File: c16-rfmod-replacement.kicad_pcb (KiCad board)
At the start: 2 copper layers, 46.6 x 38.6 mm, 21 parts, among them J1 Conn_01x04_Pin, J2 Conn_01x04_Pin, J3 Mini-DIN-4, U1 THS7314, U2 LD1117S33TR_SOT223

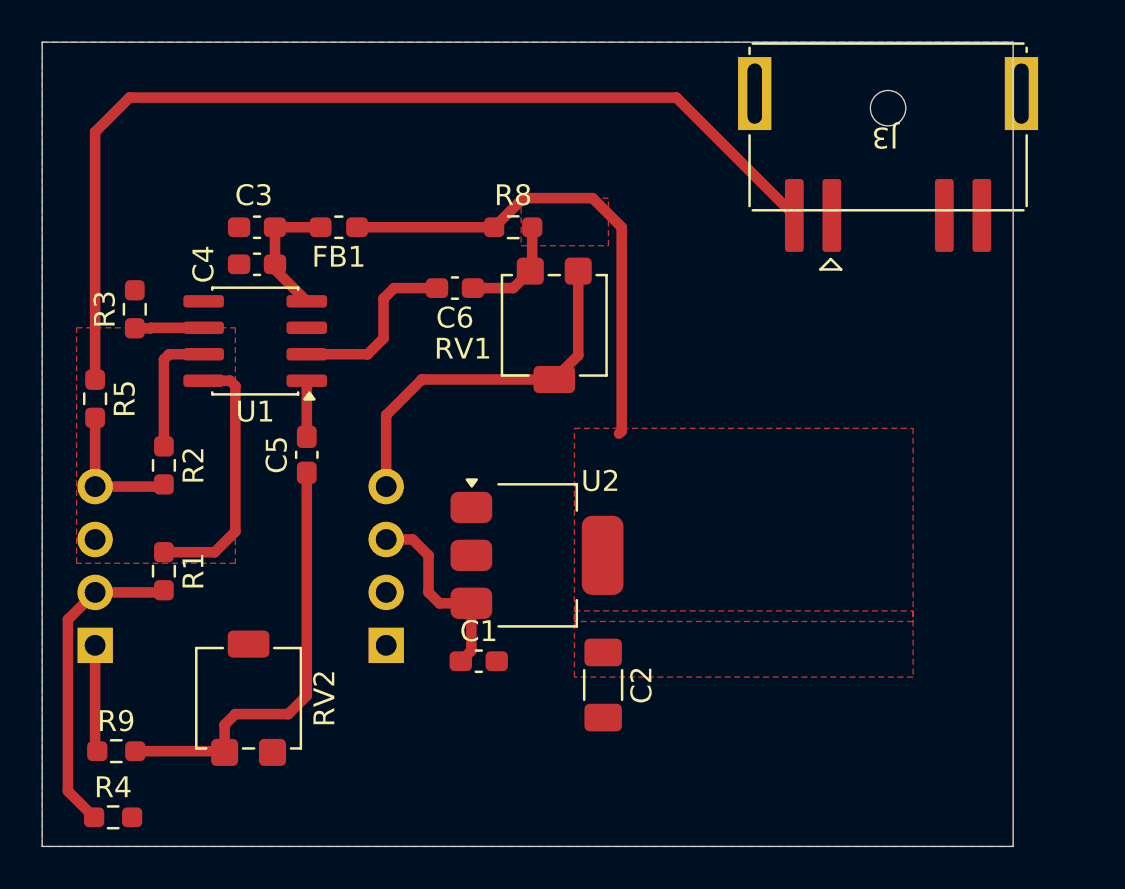
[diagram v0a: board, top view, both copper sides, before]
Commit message: C16 RF modulator replacement Rev. B
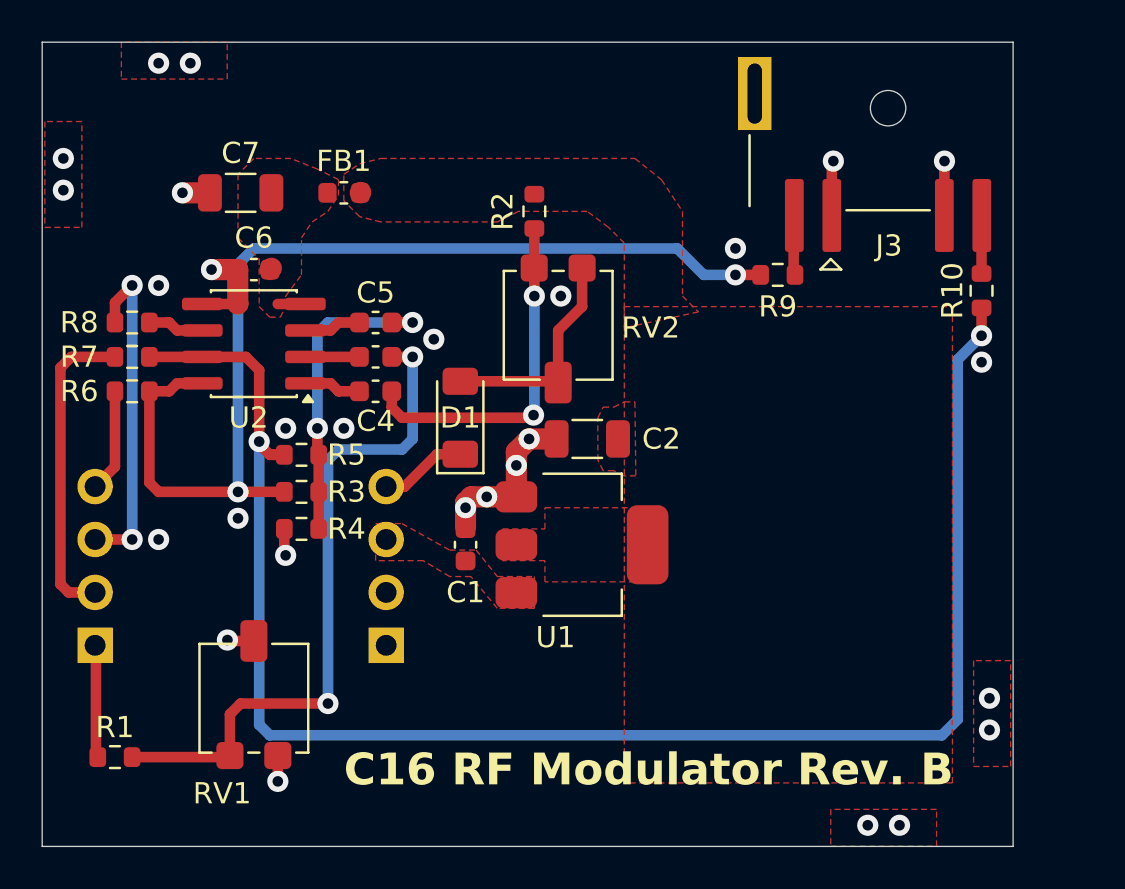
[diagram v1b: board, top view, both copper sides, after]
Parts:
- added C5: 100n, Capacitor_SMD:C_0603_1608Metric, F.Cu at (143.0, 101.9)
- added D1: 1N4148WT, Diode_SMD:D_MiniMELF, F.Cu at (147.1, 106.4)
- added R10: 75R, Resistor_SMD:R_0603_1608Metric, F.Cu at (172.1, 100.3)
- added R8: 75R, Resistor_SMD:R_0603_1608Metric, F.Cu at (131.3, 101.9)
- added R9: 75R, Resistor_SMD:R_0603_1608Metric, F.Cu at (162.3, 99.6)
- C1: footprint Capacitor_SMD:C_0603_1608Metric_Pad1.08x0.95mm_HandSolder -> Capacitor_SMD:C_0603_1608Metric
- C2: footprint Capacitor_SMD:C_1206_3216Metric_Pad1.33x1.80mm_HandSolder -> Capacitor_SMD:C_1206_3216Metric
- C3: renamed from C5; footprint Capacitor_SMD:C_0603_1608Metric_Pad1.08x0.95mm_HandSolder -> Capacitor_SMD:C_0603_1608Metric
- C4: renamed from C6; footprint Capacitor_SMD:C_0603_1608Metric_Pad1.08x0.95mm_HandSolder -> Capacitor_SMD:C_0603_1608Metric
- C6: renamed from C3; footprint Capacitor_SMD:C_0603_1608Metric_Pad1.08x0.95mm_HandSolder -> Capacitor_SMD:C_0603_1608Metric
- C7: renamed from C4; value 1u -> 47u; footprint Capacitor_SMD:C_0603_1608Metric_Pad1.08x0.95mm_HandSolder -> Capacitor_SMD:C_1206_3216Metric
- FB1: value FerriteBead_Small -> ~; footprint Inductor_SMD:L_0603_1608Metric_Pad1.05x0.95mm_HandSolder -> Inductor_SMD:L_0603_1608Metric
- J1, J2: value Conn_01x04_Pin -> C16_RFCon
- J3: value Mini-DIN-4 -> S-Video Out
- R1: renamed from R9; footprint Resistor_SMD:R_0603_1608Metric_Pad0.98x0.95mm_HandSolder -> Resistor_SMD:R_0603_1608Metric
- R2: renamed from R8; value 1k -> 220; footprint Resistor_SMD:R_0603_1608Metric_Pad0.98x0.95mm_HandSolder -> Resistor_SMD:R_0603_1608Metric
- R3: value 150R -> tbd; footprint Resistor_SMD:R_0603_1608Metric_Pad0.98x0.95mm_HandSolder -> Resistor_SMD:R_0603_1608Metric
- R4, R5: value 0 -> tbd; footprint Resistor_SMD:R_0603_1608Metric_Pad0.98x0.95mm_HandSolder -> Resistor_SMD:R_0603_1608Metric
- R6: renamed from R1; footprint Resistor_SMD:R_0603_1608Metric_Pad0.98x0.95mm_HandSolder -> Resistor_SMD:R_0603_1608Metric
- R7: renamed from R2; footprint Resistor_SMD:R_0603_1608Metric_Pad0.98x0.95mm_HandSolder -> Resistor_SMD:R_0603_1608Metric
- RV1: renamed from RV2; footprint Potentiometer_SMD:Potentiometer_Bourns_3214G_Horizontal -> Potentiometer_SMD:Potentiometer_Vishay_TS53YL_Vertical
- RV2: renamed from RV1; value 500 -> 1k; footprint Potentiometer_SMD:Potentiometer_Bourns_3214G_Horizontal -> Potentiometer_SMD:Potentiometer_Vishay_TS53YL_Vertical
- U1: renamed from U2; value LD1117S33TR_SOT223 -> LD1117S33TR
- moved R4 16.5 mm to (139.4, 111.8)
- moved R3 11.9 mm to (139.4, 110.0), turned to 180 degrees
- moved C2 11.8 mm to (153.2, 107.4), turned to 180 degrees
- moved R5 10.3 mm to (139.4, 108.2), turned to 180 degrees
- moved R6 8.77 mm to (131.3, 105.2), turned to 180 degrees
- moved C4 6.25 mm to (143.0, 105.2)
- moved C3 5.74 mm to (143.0, 103.5), turned to 180 degrees
- moved C1 5.62 mm to (147.3, 112.5), turned to 90 degrees
- moved R7 5.43 mm to (131.3, 103.5), turned to 180 degrees
- moved C7 3.52 mm to (136.5, 95.6)
- moved U1 2.22 mm to (152.9, 112.5)
- moved C6 2.04 mm to (137.2, 99.3)
- moved FB1 1.67 mm to (141.5, 95.6)
- moved R2 1.27 mm to (150.6, 96.5), turned to -90 degrees
- moved R1 0.29 mm to (130.5, 122.7)
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- renumbered U1 to U2
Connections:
- net /Chroma_IN renamed /Chroma_C16
- net Net-(C5-Pad1) renamed /Chroma_VD
- net Net-(C6-Pad1) renamed /Luma_VDOUT
- net Net-(U1-V_{S+}) renamed +3.3V_filt
- C3 pad 2: Net-(U1-CH1_IN) -> /Chroma_InTHS
- C4 pad 2: Net-(U1-CH2_IN) -> /Luma_InTHS
- J1 pad 2: /Audio_IN -> unconnected-(J1-Pin_2-Pad2)
- J1 pad 4: /Luma_IN -> /Luma_C16
- J2 pad 2: /Chroma_OUT -> Chroma_Out
- J2 pad 3: /Comp_OUT -> Comp_Out
- J2 pad 4: /Luma_Out -> Luma_Out
- J3 pad 3: Net-(J3-Pad3) -> /Luma_OutSVideo
- J3 pad 4: Net-(J3-Pad4) -> /Chroma_OutSVideo
- R3 pad 1: Net-(U1-CH3_OUT) -> /Comp_FB
- R3 pad 2: GND -> /Luma_OutTHS
- R4 pad 1: /Chroma_OUT -> GND
- R4 pad 2: Net-(J3-Pad4) -> /Comp_FB
- R5 pad 1: Net-(J3-Pad3) -> /Comp_FB
- R5 pad 2: /Luma_Out -> /Chroma_OutTHS
- R6 pad 1: Net-(U1-CH1_OUT) -> /Luma_OutTHS
- R6 pad 2: /Chroma_OUT -> Luma_Out
- R7 pad 1: Net-(U1-CH2_OUT) -> /Chroma_OutTHS
- R7 pad 2: /Luma_Out -> Chroma_Out
- RV2 pad 2: /Luma_IN -> /Luma_VDIN
- RV2 pad 3: /Luma_IN -> /Luma_VDIN
- U2 pad 1: Net-(U1-CH1_IN) -> /Luma_InTHS
- U2 pad 2: Net-(U1-CH2_IN) -> /Chroma_InTHS
- U2 pad 3: GND -> /Comp_InTHS
- U2 pad 6: Net-(U1-CH3_OUT) -> /Comp_OutTHS
- U2 pad 7: Net-(U1-CH2_OUT) -> /Chroma_OutTHS
- U2 pad 8: Net-(U1-CH1_OUT) -> /Luma_OutTHS
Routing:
- net /Chroma_OutTHS: track 0.00 -> 78.9 mm, vias 0 -> 2
- net /Luma_OutTHS: track 0.00 -> 50.6 mm, vias 0 -> 2
- net Net-(J3-Pad3): track 48.5 -> 0.00 mm
- net +3.3V: track 23.8 -> 0.03 mm
- net GND: track 0.00 -> 23.0 mm, vias 0 -> 28
- net /Luma_IN: track 17.9 -> 0.00 mm
- net Comp_Out: track 0.00 -> 16.1 mm, vias 0 -> 2
- net /Comp_FB: track 0.00 -> 15.2 mm, vias 0 -> 2
- net /Chroma_OUT: track 15.2 -> 0.00 mm
- net Chroma_Out: track 0.00 -> 15.0 mm
- net Net-(U1-CH1_OUT): track 12.5 -> 0.00 mm
- net /Chroma_VD: track 20.9 -> 32.6 mm, vias 0 -> 2
- net /Luma_VDOUT: track 5.23 -> 17.0 mm, vias 0 -> 2
- net /Luma_VDIN: track 0.00 -> 10.7 mm
- net +5V: track 9.41 -> 0.00 mm
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- added copper zone on F.Cu, net +3.3V_filt
- added copper zone on F.Cu, net +5V
- added copper zone on In1.Cu, net GND
- added copper zone on In2.Cu, net GND
- removed copper zone on F.Cu, net (none)
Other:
- copper layers 2 -> 4
- board text added: "C16 RF Modulator Rev. B"

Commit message: Rev. C - Dual Output Amplifier
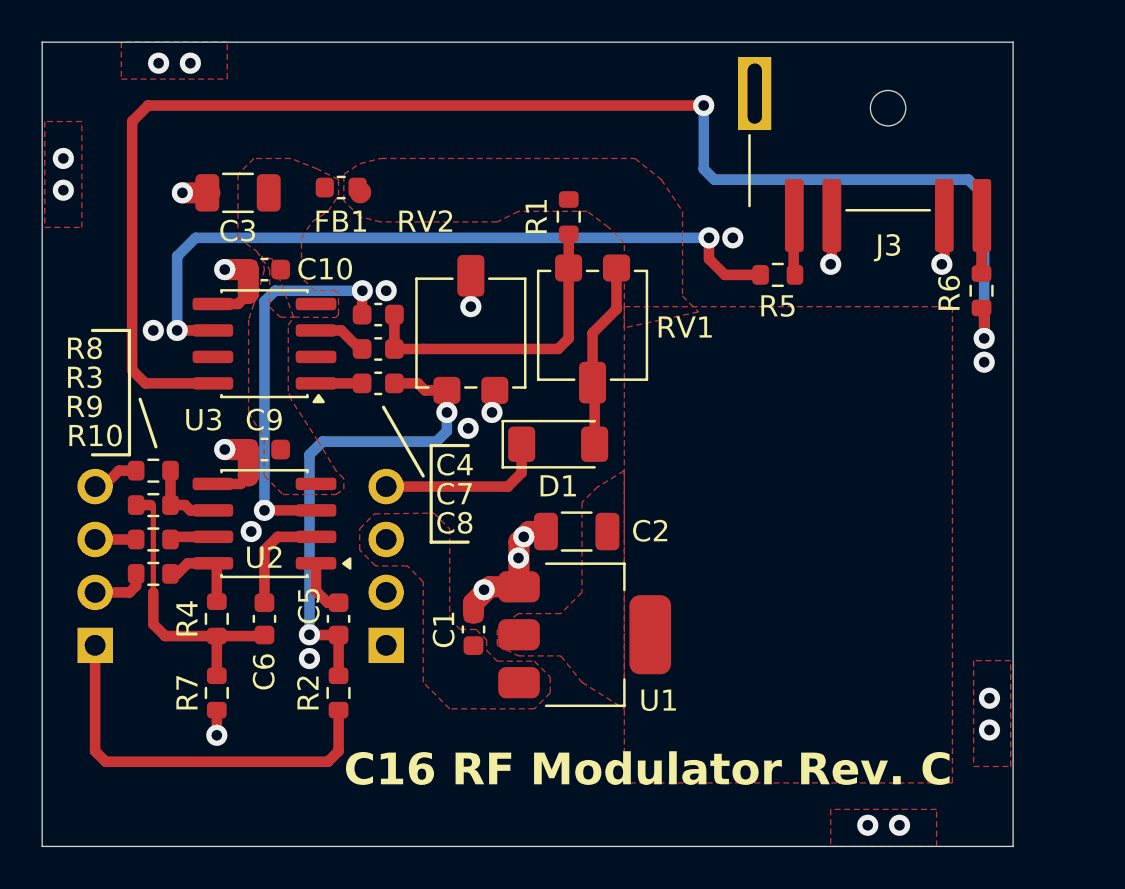
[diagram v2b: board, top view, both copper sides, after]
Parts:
- removed the C6 at (137.2, 99.3)
- removed the C7 at (136.5, 95.6)
- added C10: 10n, Capacitor_SMD:C_0603_1608Metric, F.Cu at (137.7, 99.3)
- added C3: 47u, Capacitor_SMD:C_1206_3216Metric, F.Cu at (136.4, 95.6)
- added C4: 100n, Capacitor_SMD:C_0603_1608Metric, F.Cu at (143.1, 101.5)
- added C5: 100n, Capacitor_SMD:C_0603_1608Metric, F.Cu at (141.2, 116.1)
- added C9: 10n, Capacitor_SMD:C_0603_1608Metric, F.Cu at (137.7, 108.0)
- added U3: THS7314, Package_SO:SOIC-8_3.9x4.9mm_P1.27mm, F.Cu at (137.7, 102.9)
- moved RV2 20.4 mm to (147.6, 102.4)
- moved C6 15.2 mm to (137.7, 116.1), turned to -90 degrees
- moved R2 11.2 mm to (141.2, 119.6), turned to 90 degrees
- moved R10 10.5 mm to (132.3, 113.9)
- moved R9 10.5 mm to (132.3, 112.3)
- moved R4 8.86 mm to (135.4, 116.1), turned to 90 degrees
- moved R7 8.86 mm to (135.4, 119.6), turned to 90 degrees
- moved U2 8.65 mm to (137.7, 111.5)
- moved R3 7.14 mm to (132.3, 110.6), turned to 0 degrees
- moved D1 4.87 mm to (151.8, 107.7), turned to 0 degrees
- moved C2 4.47 mm to (152.7, 111.9)
- moved U1 4.32 mm to (153.0, 116.8)
- moved C1 4.08 mm to (147.7, 116.6)
- moved R8 3.94 mm to (132.3, 109.0)
- moved C8 2.04 mm to (143.1, 103.1)
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- renumbered C5 to C6, C3 to C7, C4 to C8, R2 to R1, R7 to R10, R1 to R2, R5 to R4, R9 to R5, R10 to R6, R4 to R7, R6 to R8, R8 to R9, RV2 to RV1, RV1 to RV2
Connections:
- net /Chroma_VD renamed Chroma_In
- net /Luma_VDOUT renamed Luma_In
- C7 pad 2: /Chroma_InTHS -> /Chroma_InTHSSVIDEO
- C8 pad 2: /Luma_InTHS -> /Luma_InTHSSVIDEO
- J3 pad SH: GND -> (no net)
- R5 pad 1: /Luma_OutTHS -> /Luma_OutTHSSVideo
- R6 pad 1: /Chroma_OutTHS -> /Chroma_OutTHSSVideo
- U2 pad 1: /Luma_InTHS -> /Chroma_InTHS
- U2 pad 2: /Chroma_InTHS -> /Comp_InTHS
- U2 pad 3: /Comp_InTHS -> /Luma_InTHS
- U2 pad 6: /Comp_OutTHS -> /Luma_OutTHS
- U2 pad 7: /Chroma_OutTHS -> /Comp_OutTHS
- U2 pad 8: /Luma_OutTHS -> /Chroma_OutTHS
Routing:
- net /Chroma_OutTHS: track 78.9 -> 4.16 mm, vias 2 -> 0
- net /Chroma_OutTHSSVideo: track 0.00 -> 69.2 mm, vias 0 -> 2
- net /Luma_OutTHS: track 50.6 -> 3.79 mm, vias 2 -> 0
- net /Luma_OutTHSSVideo: track 0.00 -> 35.0 mm, vias 0 -> 2
- net /Luma_InTHS: track 2.75 -> 18.6 mm, vias 0 -> 2
- net Comp_Out: track 16.1 -> 1.97 mm, vias 2 -> 0
- net /Chroma_C16: track 5.38 -> 19.5 mm
- net Chroma_Out: track 15.0 -> 2.67 mm
- net Chroma_In: track 32.6 -> 23.7 mm
- net /Luma_C16: track 4.20 -> 8.15 mm
- net Luma_Out: track 4.97 -> 2.28 mm
- net /Luma_InTHSSVIDEO: track 0.00 -> 2.58 mm
- net /Comp_InTHS: track 2.75 -> 5.27 mm
- net /Chroma_InTHSSVIDEO: track 0.00 -> 2.21 mm
- net GND: track 23.0 -> 25.0 mm, vias 28 -> 26
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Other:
- board text added: "C16 RF Modulator Rev. C"
- board text removed: "C16 RF Modulator Rev. B"
